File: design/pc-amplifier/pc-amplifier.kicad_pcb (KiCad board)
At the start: 2 copper layers, 149.9 x 55.9 mm, 140 parts, among them J1 PJ307, J2 DC-005, J3 PJ307, J4 AV-8.4-3, J5 AV-8.4-3, K1 HK19F-DC-12-SHG, Q1 BC858, Q2 BC817, Q3 BC817, Q4 BC817, SW1 6mm Tactile SW, SW2 6mm Tactile SW, SW3 6mm Tactile SW, SW4 6mm Tactile SW, U1 TDA8425, U2 NE5532, U3 NE5532, U4 NE5532, U5 YDA138, U6 MC78L05, U7 AC6939-MODULE

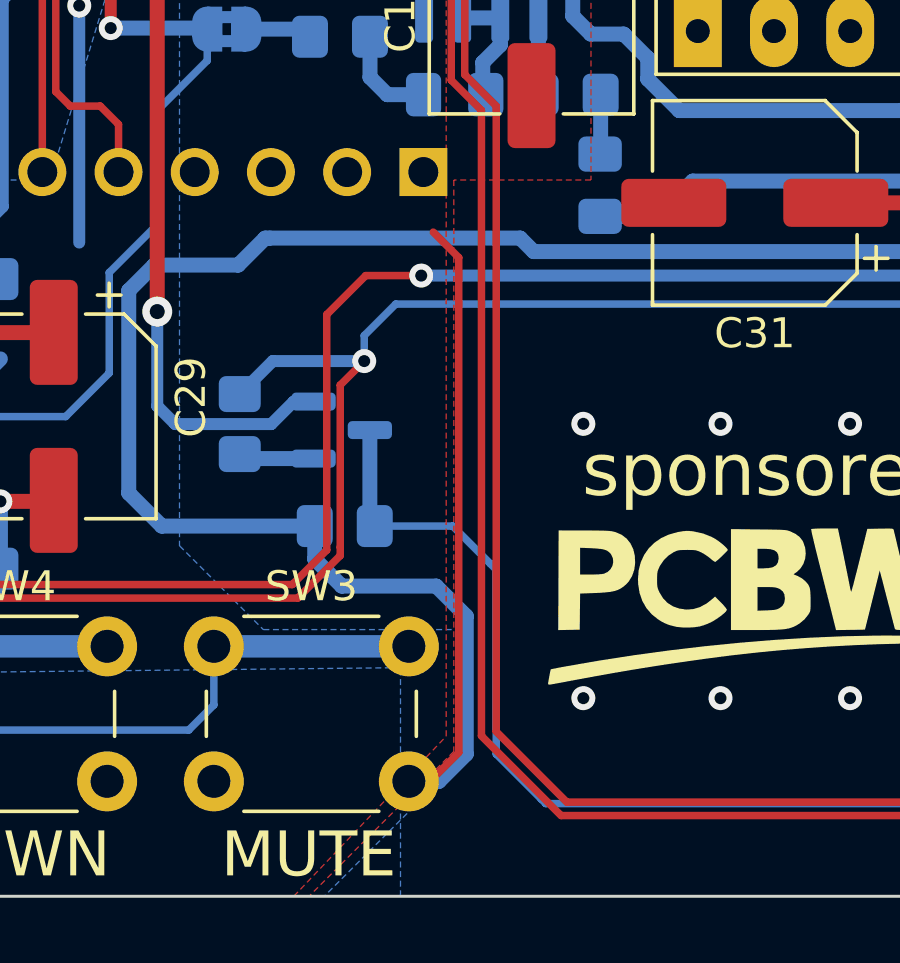
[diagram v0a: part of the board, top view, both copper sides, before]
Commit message: Fix fill issue in GNDD top layer.
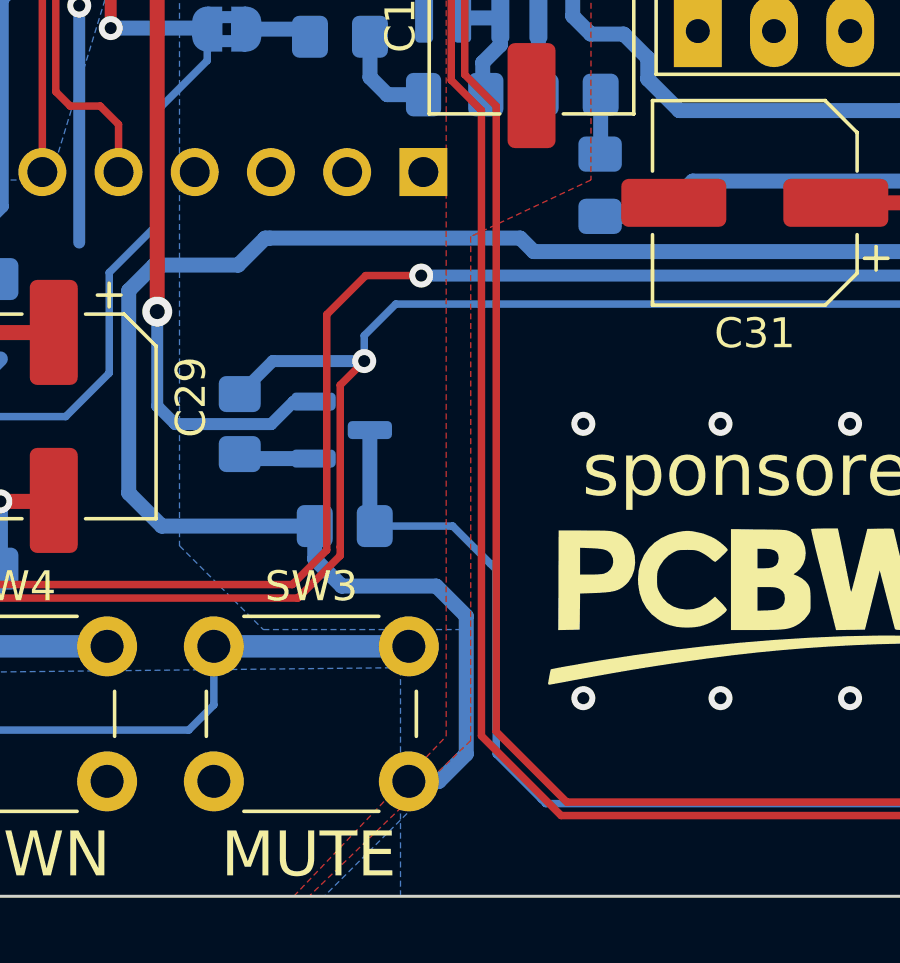
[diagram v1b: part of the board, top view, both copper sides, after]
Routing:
- net GNDD: track 333.2 -> 314.1 mm
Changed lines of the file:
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@@
   (segment (start 172.7902 114.2402) (end 173.25 114.7) (width 0.4) (layer "F.Cu") (net 7))
   (segment (start 107.81 74.8125) (end 107.81 73.39) (width 0.25) (layer "F.Cu") (net 7))
-  (segment (start 118.4412 119.3588) (end 119.4 118.4) (width 0.25) (layer "F.Cu") (net 7))
   (segment (start 167.275 118.525) (end 166.65 117.9) (width 0.5) (layer "F.Cu") (net 7))
   (segment (start 208.05 100.75) (end 203.85 100.75) (width 0.5) (layer "F.Cu") (net 7))
@@
   (segment (start 174.35 111.2) (end 174.35 112.85) (width 0.4) (layer "F.Cu") (net 7))
   (segment (start 175.725 114.675) (end 176.2 114.2) (width 0.4) (layer "F.Cu") (net 7))
-  (segment (start 119.4 118.4) (end 119.4 101.9) (width 0.25) (layer "F.Cu") (net 7))
-  (segment (start 119.4 101.9) (end 118.55 101.05) (width 0.25) (layer "F.Cu") (net 7))
   (segment (start 159.65 109.4) (end 159.65 110) (width 0.5) (layer "F.Cu") (net 7))
   (segment (start 186.15 112.85) (end 186.075 112.775) (width 0.4) (layer "F.Cu") (net 7))
@@
         (xy 123.808 85.09)
         (xy 123.808 99.314)
-        (xy 119.236 99.314)
-        (xy 119.236 118.364)
+        (xy 119.8 101.2)
+        (xy 119.8 118)
         (xy 114.41 123.19)
         (xy 75.04 123.19)
